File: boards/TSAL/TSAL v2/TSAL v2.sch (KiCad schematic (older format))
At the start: 17 parts, among them Q1 BSS308PE, U1 LR8K4-G, U2 OPA340NA, U3 LTV-356T

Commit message: Changes to TSAL v2
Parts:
- added C1: C_1uF, footprints:C_0805_OEM, symbol C_1uF
- added C2: C_10uF, footprints:C_0805_OEM, symbol C_10uF
- added C?: C_0.1uF, footprints:C_0805_OEM, symbol C_0.1uF
- added C?: C_22uF, footprints:C_1206_OEM, symbol C_22uF
- added C?: C_47uF, footprints:C_0805_OEM, symbol C_47uF
- added D? (x2): LED_0805, footprints:LED_0805_OEM, symbol LED_0805
- added D?: D_Zener_18V, footprints:DO-214AA, symbol D_Zener_18V
- added F?: F_500mA_16V, footprints:Fuse_1210, symbol F_500mA_16V
- added L?: L_4.7uH, footprints:4.7uH_Inductor_OEM, symbol L_4.7uH
- added R11, R12, R?: R_1k, footprints:R_0805_OEM, symbol R_1k
- added R? (x2): R_10k, footprints:R_0805_OEM, symbol R_10k
- added R?: R_55.1k, footprints:R_0805_OEM, symbol R_55.1k
- added R?: R_200, footprints:R_0805_OEM, symbol R_200
- added R?: R_0_Jumper, footprints:R_2512_OEM, symbol R_0_Jumper
- added U?: TPS561201, footprints:SOT-23-6_OEM, symbol TPS561201
- renumbered R11 to R13
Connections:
- net labels added: +12V, 12V_Fused, 5V, VCC
- net labels removed: +5V
- wire segments 58 -> 80
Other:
- note added: "(5V)"
- note added: "12V Indicator"
- note added: "5V Indicator"
- note added: "Add Precision Reference here"
- note added: "BUCK CONVERTER"
- note added: "Use a 100:1 voltage divider here"
- moved on the sheet: D1, R13, R6, U1, U3

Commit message: Final TSAL v2 schematic
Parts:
- removed C?: C_0.1uF, footprints:C_0805_OEM, symbol C_0.1uF
- removed C?: C_22uF, footprints:C_1206_OEM, symbol C_22uF
- removed C?: C_47uF, footprints:C_0805_OEM, symbol C_47uF
- removed D? (x2): LED_0805, footprints:LED_0805_OEM, symbol LED_0805
- removed D?: D_Zener_18V, footprints:DO-214AA, symbol D_Zener_18V
- removed F1: 200mA_Fuse, symbol 200mA_Fuse
- removed F?: F_500mA_16V, footprints:Fuse_1210, symbol F_500mA_16V
- removed L?: L_4.7uH, footprints:4.7uH_Inductor_OEM, symbol L_4.7uH
- removed Q1: BSS308PE, TO_SOT_Packages_SMD:SOT-23, symbol BSS308PE
- removed R1: R_3k_HS, footprints:R_3k_HS_TO247, symbol R_3k_HS
- removed R10: R_2.94M, footprints:R_0805_OEM, symbol R_2.94M
- removed R12, R?: R_1k, footprints:R_0805_OEM, symbol R_1k
- removed R2: R_1k_HS, footprints:R_1k_HS_TO247, symbol R_1k_HS
- removed R3, R4, R5: R_1M, footprints:R_0805_OEM, symbol R_1M
- removed R6, R? (x2): R_10k, footprints:R_0805_OEM, symbol R_10k
- removed R7: R_3.01k, footprints:R_0805_OEM, symbol R_3.01k
- removed R8, R9: R_22M, footprints:R_0805_OEM, symbol R_22M
- removed R?: R_55.1k, footprints:R_0805_OEM, symbol R_55.1k
- removed R?: R_200, footprints:R_0805_OEM, symbol R_200
- removed R?: R_0_Jumper, footprints:R_2512_OEM, symbol R_0_Jumper
- removed U2: OPA340NA, symbol OPA340NA
- removed U?: TPS561201, footprints:SOT-23-6_OEM, symbol TPS561201
- added C2: C_1uF, footprints:C_0805_OEM, symbol C_1uF
- added C3: C_0.1uF, footprints:C_0805_OEM, symbol C_0.1uF
- added F1: F_21mA_420V, footprints:F_21mA_420V, symbol F_21mA_420V
- added J1, J2: Ultrafit_2, footprints:Ultrafit_2, symbol Ultrafit_2
- added J3: micromatch_female_RA_4, footprints:micromatch_female_ra_4, symbol micromatch_female_RA_4
- added Q1: NMOS_GSD_30V, TO_SOT_Packages_SMD:SOT-23, symbol NMOS_GSD_30V
- added R1: R_3k, footprints:R_0805_OEM, symbol R_3k
- added R10: R_499, footprints:R_0805_OEM, symbol R_499
- added R2, R8: R_1k, footprints:R_0805_OEM, symbol R_1k
- added R3, R4, R6: R_270k, footprints:R_0805_OEM, symbol R_270k
- added R5: R_10k, footprints:R_0805_OEM, symbol R_10k
- added R7: R_178k, footprints:R_0805_OEM, symbol R_178k
- added U2: ZXRE160, footprints:ZXRE160, symbol ZXRE160
- added U3: MCP6001RT, footprints:SOT-23-5_OEM, symbol MCP6001RT
- U1: footprint Package_TO_SOT_SMD:TO-252-2 -> TO_SOT_Packages_SMD:TO-252-3_TabPin2; MFN (none) -> Mouser; MPN (none) -> 689-LR8K4-G; Webpage (none) -> https://www.mouser.com/productdetail/?qs=jWmFlM7coATgElKtQd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
- renumbered C2 to C4, R13 to R11, R11 to R9, U3 to U4
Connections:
- net labels removed: +12V, 12V_Fused, 5V
- wire segments 80 -> 77
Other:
- note removed: "(5V)"
- note removed: "12V Indicator"
- note removed: "5V Indicator"
- note removed: "Add Precision Reference here"
- note removed: "BUCK CONVERTER"
- note removed: "Use a 100:1 voltage divider here"
- moved on the sheet: C1, C4, D1, R11, R9, U4

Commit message: Adding TSAL v2 final schematic
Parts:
- J3: symbol micromatch_female_RA_4 -> micromatch_female_RA_4-RESCUE-TSAL_v2
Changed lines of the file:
@@
 $EndComp
 $Comp
-L micromatch_female_RA_4 J3
+L micromatch_female_RA_4-RESCUE-TSAL_v2 J3
 U 1 1 5A73FCF8
 P 10400 2300

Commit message: BOM, Netlist, PCB final
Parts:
- removed J3: micromatch_female_RA_4, footprints:micromatch_female_ra_4, symbol micromatch_female_RA_4-RESCUE-TSAL_v2
- added J3: micromatch_female_TOP_ENTRY_locking_4, footprints:micromatch_female_vert_4, symbol micromatch_female_TOP_ENTRY_locking_4
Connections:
- net VCC is gone; now on net GLV+: U4.4
- net GLV+: now also J3.2, J3.3
- net GND: now also J3.1; no longer C1.2
- net TS-: now also C1.2
- net TSAL-: now also J3.4
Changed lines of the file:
@@
-	1    0    0    -1
-$EndComp
-$Comp
-L GND #PWR03
-U 1 1 5A6AABDC
-P 3850 4900
-F 0 "#PWR03" H 3850 4650 50  0001 C CNN
-F 1 "GND" H 3850 4750 50  0000 C CNN
-F 2 "" H 3850 4900 50  0001 C CNN
-F 3 "" H 3850 4900 50  0001 C CNN
-	1    3850 4900
 	1    0    0    -1
 $EndComp
@@
 5V_TS
 $Comp
-L VCC #PWR04
-U 1 1 5A73F060
-P 12600 3850
-F 0 "#PWR04" H 12600 3700 50  0001 C CNN
-F 1 "VCC" H 12600 4000 50  0000 C CNN
-F 2 "" H 12600 3850 50  0001 C CNN
-F 3 "" H 12600 3850 50  0001 C CNN
-	1    12600 3850
-	1    0    0    -1
-$EndComp
-$Comp
-L micromatch_female_RA_4-RESCUE-TSAL_v2 J3
-U 1 1 5A73FCF8
-P 10400 2300
-F 0 "J3" H 10300 3500 60  0000 C CNN
-F 1 "micromatch_female_RA_4" V 10050 3250 60  0000 C CNN
-F 2 "footprints:micromatch_female_ra_4" H 10200 3400 60  0001 C CNN
-F 3 "" H 10300 3500 60  0001 C CNN
-F 4 "https://www.digikey.com/product-detail/en/te-connectivity-amp-connectors/338070-4/A99482CT-ND/1955784" H 10400 3600 60  0001 C CNN "PurchasingLink"
-F 5 "Digi-Key" H 10500 3700 60  0001 C CNN "MFN"
-F 6 "A99482CT-ND" H 10600 3800 60  0001 C CNN "MPN"
-F 7 "Value" H 10700 3900 60  0001 C CNN "Package"
-	1    10400 2300
-	0    1    1    0
-$EndComp
-$Comp
 L Ultrafit_2 J1
 U 1 1 5A7400DA
@@
 	4100 3800 3950 3800
 Wire Wire Line
-	2200 5700 3000 5700
+	3850 5700 2200 5700
 Wire Wire Line
 	3000 5700 3000 5400
@@
 Connection ~ 3850 4250
 Wire Wire Line
-	3850 4800 3850 4900
+	3850 4800 3850 5700
 Wire Notes Line
 	4800 6650 10100 6650
@@
 	2200 4200 2050 4200
 Wire Wire Line
-	2200 4300 2200 5700
-Wire Wire Line
-	2050 4300 2200 4300
+	2200 5700 2200 4300
+Wire Wire Line
+	2200 4300 2050 4300
 Text GLabel 2200 3050 0    60   Input ~ 0
 TS+
-Text GLabel 10850 2650 0    60   Input ~ 0
+Text GLabel 14150 6700 0    60   Input ~ 0
 TSAL-
 Wire Wire Line
-	10850 2650 11200 2650
-Wire Wire Line
-	11200 2650 11200 2450
-Text GLabel 10850 3000 0    60   Input ~ 0
+	14150 6700 14500 6700
+Wire Wire Line
+	14500 6700 14500 6500
+Text GLabel 14150 7050 0    60   Input ~ 0
 TSAL+
 Wire Wire Line
-	10850 3000 11300 3000
-Wire Wire Line
-	11300 3000 11300 2450
-Text GLabel 11750 3000 2    60   Input ~ 0
+	14150 7050 14600 7050
+Wire Wire Line
+	14600 7050 14600 6500
+Text GLabel 15050 7050 2    60   Input ~ 0
 GLV+
 $Comp
-L GND #PWR05
+L GND #PWR03
 U 1 1 5A741A32
-P 11500 2450
-F 0 "#PWR05" H 11500 2200 50  0001 C CNN
-F 1 "GND" H 11500 2300 50  0000 C CNN
-F 2 "" H 11500 2450 50  0001 C CNN
-F 3 "" H 11500 2450 50  0001 C CNN
-	1    11500 2450
-	1    0    0    -1
-$EndComp
-Wire Wire Line
-	11400 2450 11400 3000
-Wire Wire Line
-	11400 3000 11750 3000
+P 14800 6500
+F 0 "#PWR03" H 14800 6250 50  0001 C CNN
+F 1 "GND" H 14800 6350 50  0000 C CNN
+F 2 "" H 14800 6500 50  0001 C CNN
+F 3 "" H 14800 6500 50  0001 C CNN
+	1    14800 6500
+	1    0    0    -1
+$EndComp
+Wire Wire Line
+	14700 6500 14700 7050
+Wire Wire Line
+	14700 7050 15050 7050
 Wire Notes Line
 	15350 5550 15350 2800
@@
 Connection ~ 10950 4400
 $Comp
-L PWR_FLAG #FLG06
-U 1 1 5A76BFCE
-P 13800 1750
-F 0 "#FLG06" H 13800 1825 50  0001 C CNN
-F 1 "PWR_FLAG" H 13800 1900 50  0000 C CNN
-F 2 "" H 13800 1750 50  0001 C CNN
-F 3 "" H 13800 1750 50  0001 C CNN
-	1    13800 1750
-	1    0    0    -1
-$EndComp
-$Comp
-L VCC #PWR07
-U 1 1 5A76C05D
-P 13800 1750
-F 0 "#PWR07" H 13800 1600 50  0001 C CNN
-F 1 "VCC" H 13800 1900 50  0000 C CNN
-F 2 "" H 13800 1750 50  0001 C CNN
-F 3 "" H 13800 1750 50  0001 C CNN
-	1    13800 1750
-	-1   0    0    1
-$EndComp
-$Comp
-L PWR_FLAG #FLG08
+L PWR_FLAG #FLG04
 U 1 1 5A76C4FF
 P 14200 1750
-F 0 "#FLG08" H 14200 1825 50  0001 C CNN
+F 0 "#FLG04" H 14200 1825 50  0001 C CNN
 F 1 "PWR_FLAG" H 14200 1900 50  0000 C CNN
 F 2 "" H 14200 1750 50  0001 C CNN
@@
 $EndComp
 $Comp
-L PWR_FLAG #FLG09
+L PWR_FLAG #FLG05
 U 1 1 5A76C5DC
 P 14600 1750
-F 0 "#FLG09" H 14600 1825 50  0001 C CNN
+F 0 "#FLG05" H 14600 1825 50  0001 C CNN
 F 1 "PWR_FLAG" H 14600 1900 50  0000 C CNN
 F 2 "" H 14600 1750 50  0001 C CNN
@@
 $EndComp
 $Comp
-L PWR_FLAG #FLG010
+L PWR_FLAG #FLG06
 U 1 1 5A76C632
 P 15000 1750
-F 0 "#FLG010" H 15000 1825 50  0001 C CNN
+F 0 "#FLG06" H 15000 1825 50  0001 C CNN
 F 1 "PWR_FLAG" H 15000 1900 50  0000 C CNN
 F 2 "" H 15000 1750 50  0001 C CNN
@@
 TS+
 $Comp
-L GND #PWR011
+L GND #PWR07
 U 1 1 5A76CA1A
 P 15000 1750
-F 0 "#PWR011" H 15000 1500 50  0001 C CNN
+F 0 "#PWR07" H 15000 1500 50  0001 C CNN
 F 1 "GND" H 15000 1600 50  0000 C CNN
 F 2 "" H 15000 1750 50  0001 C CNN
@@
 	1    0    0    -1
 $EndComp
+$Comp
+L micromatch_female_TOP_ENTRY_locking_4 J3
+U 1 1 5A78D935
+P 14600 6250
+F 0 "J3" H 14600 6650 60  0000 C CNN
+F 1 "micromatch_female_TOP_ENTRY_locking_4" V 14350 6250 60  0000 C CNN
+F 2 "footprints:micromatch_female_vert_4" H 14400 7350 60  0001 C CNN
+F 3 "http://www.te.com/commerce/DocumentDelivery/DDEController?Action=srchrtrv&DocNm=338068&DocType=Customer+Drawing&DocLang=English" H 14500 7450 60  0001 C CNN
+F 4 "https://www.digikey.com/product-detail/en/te-connectivity-amp-connectors/338068-4/A99438CT-ND/1955740" H 14600 7550 60  0001 C CNN "PurchasingLink"
+F 5 "Digi-Key" H 14700 7650 60  0001 C CNN "MFN"
+F 6 "338068-4" H 14800 7750 60  0001 C CNN "MPN"
+F 7 "Value" H 14900 7850 60  0001 C CNN "Package"
+	1    14600 6250
+	0    1    1    0
+$EndComp
+Text GLabel 12600 3850 2    60   Input ~ 0
+GLV+
+Connection ~ 3000 5700
 $EndSCHEMATC

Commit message: Final maybe..?
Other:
- note added: "MISC"
- moved on the sheet: J3
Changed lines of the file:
@@
 Text GLabel 2200 3050 0    60   Input ~ 0
 TS+
-Text GLabel 14150 6700 0    60   Input ~ 0
+Text GLabel 7350 8650 0    60   Input ~ 0
 TSAL-
 Wire Wire Line
-	14150 6700 14500 6700
-Wire Wire Line
-	14500 6700 14500 6500
-Text GLabel 14150 7050 0    60   Input ~ 0
+	7350 8650 7700 8650
+Wire Wire Line
+	7700 8650 7700 8450
+Text GLabel 7350 9000 0    60   Input ~ 0
 TSAL+
 Wire Wire Line
-	14150 7050 14600 7050
-Wire Wire Line
-	14600 7050 14600 6500
-Text GLabel 15050 7050 2    60   Input ~ 0
+	7350 9000 7800 9000
+Wire Wire Line
+	7800 9000 7800 8450
+Text GLabel 8250 9000 2    60   Input ~ 0
 GLV+
 $Comp
 L GND #PWR03
 U 1 1 5A741A32
-P 14800 6500
-F 0 "#PWR03" H 14800 6250 50  0001 C CNN
-F 1 "GND" H 14800 6350 50  0000 C CNN
-F 2 "" H 14800 6500 50  0001 C CNN
-F 3 "" H 14800 6500 50  0001 C CNN
-	1    14800 6500
-	1    0    0    -1
-$EndComp
-Wire Wire Line
-	14700 6500 14700 7050
-Wire Wire Line
-	14700 7050 15050 7050
+P 8000 8450
+F 0 "#PWR03" H 8000 8200 50  0001 C CNN
+F 1 "GND" H 8000 8300 50  0000 C CNN
+F 2 "" H 8000 8450 50  0001 C CNN
+F 3 "" H 8000 8450 50  0001 C CNN
+	1    8000 8450
+	1    0    0    -1
+$EndComp
+Wire Wire Line
+	7900 8450 7900 9000
+Wire Wire Line
+	7900 9000 8250 9000
 Wire Notes Line
 	15350 5550 15350 2800
@@
 L PWR_FLAG #FLG04
 U 1 1 5A76C4FF
-P 14200 1750
-F 0 "#FLG04" H 14200 1825 50  0001 C CNN
-F 1 "PWR_FLAG" H 14200 1900 50  0000 C CNN
-F 2 "" H 14200 1750 50  0001 C CNN
-F 3 "" H 14200 1750 50  0001 C CNN
-	1    14200 1750
+P 9300 8400
+F 0 "#FLG04" H 9300 8475 50  0001 C CNN
+F 1 "PWR_FLAG" H 9300 8550 50  0000 C CNN
+F 2 "" H 9300 8400 50  0001 C CNN
+F 3 "" H 9300 8400 50  0001 C CNN
+	1    9300 8400
 	1    0    0    -1
 $EndComp
@@
 L PWR_FLAG #FLG05
 U 1 1 5A76C5DC
-P 14600 1750
-F 0 "#FLG05" H 14600 1825 50  0001 C CNN
-F 1 "PWR_FLAG" H 14600 1900 50  0000 C CNN
-F 2 "" H 14600 1750 50  0001 C CNN
-F 3 "" H 14600 1750 50  0001 C CNN
-	1    14600 1750
+P 9700 8400
+F 0 "#FLG05" H 9700 8475 50  0001 C CNN
+F 1 "PWR_FLAG" H 9700 8550 50  0000 C CNN
+F 2 "" H 9700 8400 50  0001 C CNN
+F 3 "" H 9700 8400 50  0001 C CNN
+	1    9700 8400
 	1    0    0    -1
 $EndComp
@@
 L PWR_FLAG #FLG06
 U 1 1 5A76C632
-P 15000 1750
-F 0 "#FLG06" H 15000 1825 50  0001 C CNN
-F 1 "PWR_FLAG" H 15000 1900 50  0000 C CNN
-F 2 "" H 15000 1750 50  0001 C CNN
-F 3 "" H 15000 1750 50  0001 C CNN
-	1    15000 1750
-	1    0    0    -1
-$EndComp
-Text GLabel 14600 1750 3    60   Input ~ 0
+P 10100 8400
+F 0 "#FLG06" H 10100 8475 50  0001 C CNN
+F 1 "PWR_FLAG" H 10100 8550 50  0000 C CNN
+F 2 "" H 10100 8400 50  0001 C CNN
+F 3 "" H 10100 8400 50  0001 C CNN
+	1    10100 8400
+	1    0    0    -1
+$EndComp
+Text GLabel 9700 8400 3    60   Input ~ 0
 TS-
-Text GLabel 14200 1750 3    60   Input ~ 0
+Text GLabel 9300 8400 3    60   Input ~ 0
 TS+
 $Comp
 L GND #PWR07
 U 1 1 5A76CA1A
-P 15000 1750
-F 0 "#PWR07" H 15000 1500 50  0001 C CNN
-F 1 "GND" H 15000 1600 50  0000 C CNN
-F 2 "" H 15000 1750 50  0001 C CNN
-F 3 "" H 15000 1750 50  0001 C CNN
-	1    15000 1750
+P 10100 8400
+F 0 "#PWR07" H 10100 8150 50  0001 C CNN
+F 1 "GND" H 10100 8250 50  0000 C CNN
+F 2 "" H 10100 8400 50  0001 C CNN
+F 3 "" H 10100 8400 50  0001 C CNN
+	1    10100 8400
 	1    0    0    -1
 $EndComp
@@
 L micromatch_female_TOP_ENTRY_locking_4 J3
 U 1 1 5A78D935
-P 14600 6250
-F 0 "J3" H 14600 6650 60  0000 C CNN
-F 1 "micromatch_female_TOP_ENTRY_locking_4" V 14350 6250 60  0000 C CNN
-F 2 "footprints:micromatch_female_vert_4" H 14400 7350 60  0001 C CNN
-F 3 "http://www.te.com/commerce/DocumentDelivery/DDEController?Action=srchrtrv&DocNm=338068&DocType=Customer+Drawing&DocLang=English" H 14500 7450 60  0001 C CNN
-F 4 "https://www.digikey.com/product-detail/en/te-connectivity-amp-connectors/338068-4/A99438CT-ND/1955740" H 14600 7550 60  0001 C CNN "PurchasingLink"
-F 5 "Digi-Key" H 14700 7650 60  0001 C CNN "MFN"
-F 6 "338068-4" H 14800 7750 60  0001 C CNN "MPN"
-F 7 "Value" H 14900 7850 60  0001 C CNN "Package"
-	1    14600 6250
+P 7800 8200
+F 0 "J3" H 7800 8600 60  0000 C CNN
+F 1 "micromatch_female_TOP_ENTRY_locking_4" V 7550 8200 60  0000 C CNN
+F 2 "footprints:micromatch_female_vert_4" H 7600 9300 60  0001 C CNN
+F 3 "http://www.te.com/commerce/DocumentDelivery/DDEController?Action=srchrtrv&DocNm=338068&DocType=Customer+Drawing&DocLang=English" H 7700 9400 60  0001 C CNN
+F 4 "https://www.digikey.com/product-detail/en/te-connectivity-amp-connectors/338068-4/A99438CT-ND/1955740" H 7800 9500 60  0001 C CNN "PurchasingLink"
+F 5 "Digi-Key" H 7900 9600 60  0001 C CNN "MFN"
+F 6 "338068-4" H 8000 9700 60  0001 C CNN "MPN"
+F 7 "Value" H 8100 9800 60  0001 C CNN "Package"
+	1    7800 8200
 	0    1    1    0
 $EndComp
@@
 GLV+
 Connection ~ 3000 5700
+Text Notes 8350 7650 0    118  ~ 24
+MISC
+Wire Notes Line
+	6700 7800 10450 7800
+Wire Notes Line
+	10450 7800 10450 9250
+Wire Notes Line
+	10450 9250 6700 9250
+Wire Notes Line
+	6700 9250 6700 7800
 $EndSCHEMATC

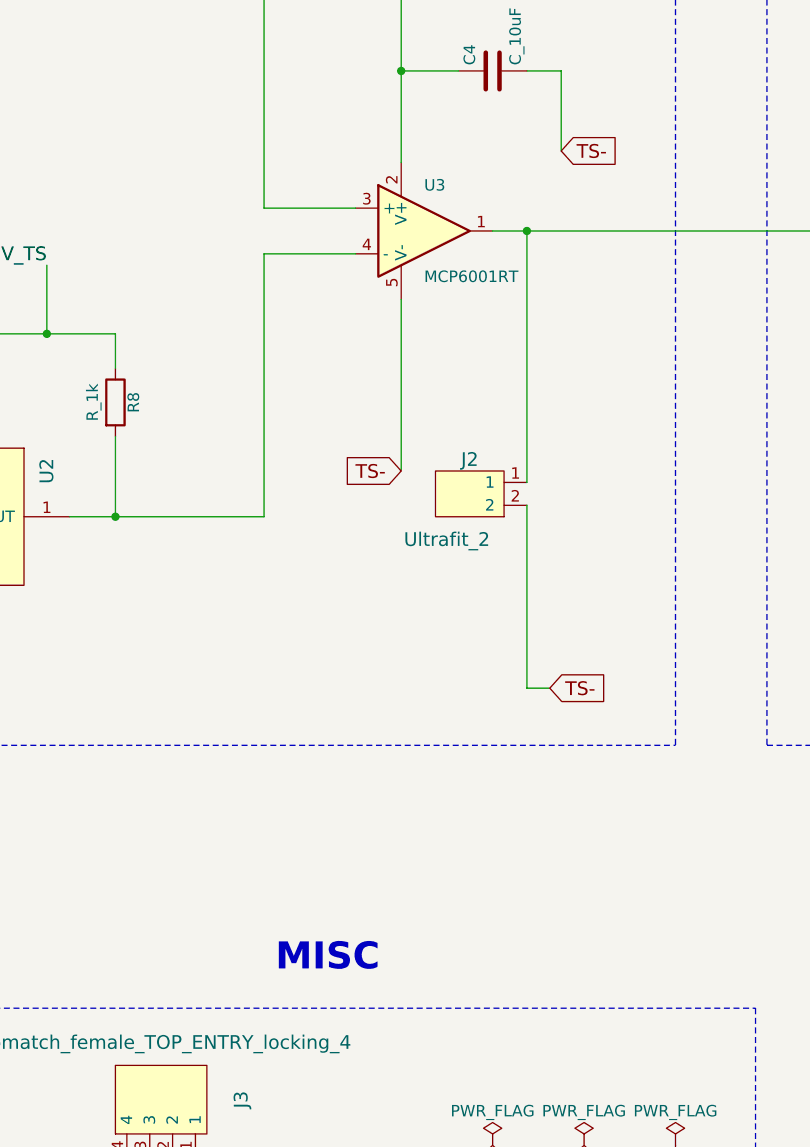
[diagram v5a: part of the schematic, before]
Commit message: Added 1.43k res for AIL
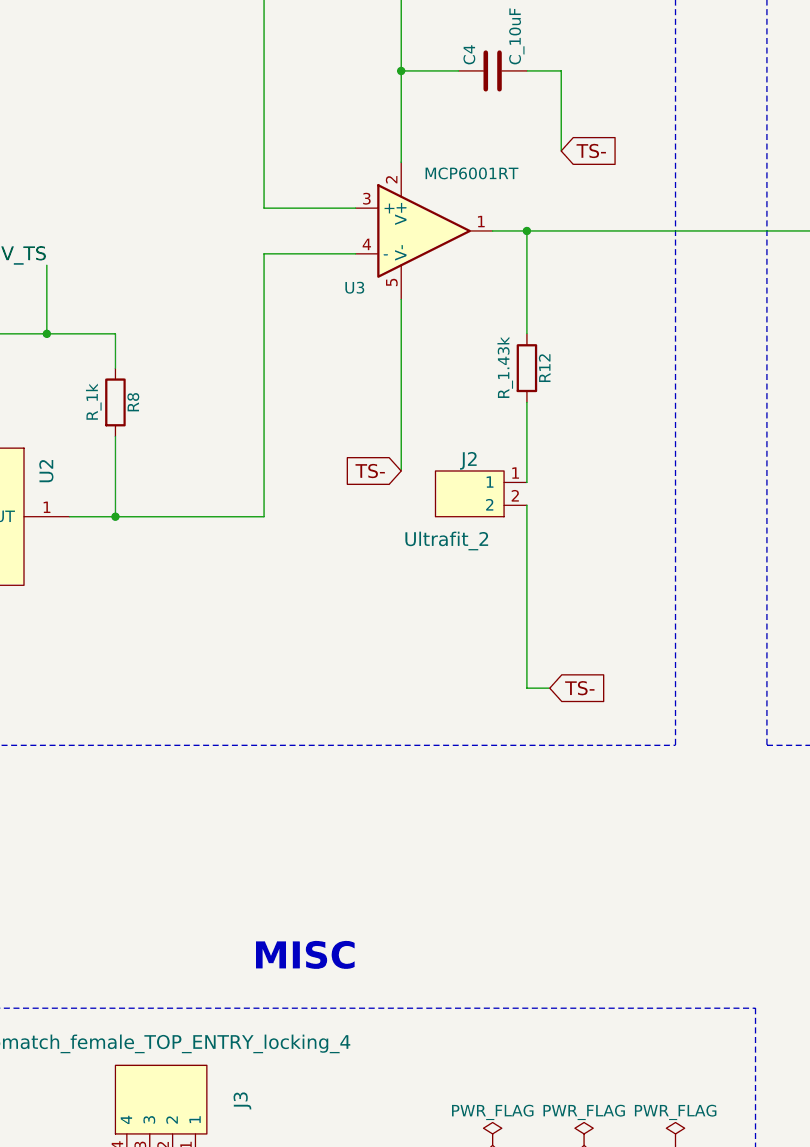
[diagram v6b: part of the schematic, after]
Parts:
- added R12: R_1.43k, footprints:R_0805_OEM, symbol R_1.43k
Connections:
- net at D1.2 (A), R10.2, U3.1: now also R12.1; no longer J2.1
- new net: J2.1, R12.2
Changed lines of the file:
@@
 $EndComp
 $Comp
-L GND #PWR01
+L GND #PWR3
 U 1 1 5A4D7FE1
 P 12600 5250
-F 0 "#PWR01" H 12600 5000 50  0001 C CNN
+F 0 "#PWR3" H 12600 5000 50  0001 C CNN
 F 1 "GND" H 12600 5100 50  0000 C CNN
 F 2 "" H 12600 5250 50  0001 C CNN
@@
 $EndComp
 $Comp
-L GND #PWR02
+L GND #PWR4
 U 1 1 5A4D80CB
 P 14200 4950
-F 0 "#PWR02" H 14200 4700 50  0001 C CNN
+F 0 "#PWR4" H 14200 4700 50  0001 C CNN
 F 1 "GND" H 14200 4800 50  0000 C CNN
 F 2 "" H 14200 4950 50  0001 C CNN
@@
 GLV+
 $Comp
-L GND #PWR03
+L GND #PWR1
 U 1 1 5A741A32
 P 8000 8450
-F 0 "#PWR03" H 8000 8200 50  0001 C CNN
+F 0 "#PWR1" H 8000 8200 50  0001 C CNN
 F 1 "GND" H 8000 8300 50  0000 C CNN
 F 2 "" H 8000 8450 50  0001 C CNN
@@
 Wire Wire Line
 	7000 2550 7150 2550
-Wire Wire Line
-	9450 5500 9450 4400
 Connection ~ 9450 4400
 Wire Wire Line
@@
 Connection ~ 10950 4400
 $Comp
-L PWR_FLAG #FLG04
+L PWR_FLAG #FLG1
 U 1 1 5A76C4FF
 P 9300 8400
-F 0 "#FLG04" H 9300 8475 50  0001 C CNN
+F 0 "#FLG1" H 9300 8475 50  0001 C CNN
 F 1 "PWR_FLAG" H 9300 8550 50  0000 C CNN
 F 2 "" H 9300 8400 50  0001 C CNN
@@
 $EndComp
 $Comp
-L PWR_FLAG #FLG05
+L PWR_FLAG #FLG2
 U 1 1 5A76C5DC
 P 9700 8400
-F 0 "#FLG05" H 9700 8475 50  0001 C CNN
+F 0 "#FLG2" H 9700 8475 50  0001 C CNN
 F 1 "PWR_FLAG" H 9700 8550 50  0000 C CNN
 F 2 "" H 9700 8400 50  0001 C CNN
@@
 $EndComp
 $Comp
-L PWR_FLAG #FLG06
+L PWR_FLAG #FLG3
 U 1 1 5A76C632
 P 10100 8400
-F 0 "#FLG06" H 10100 8475 50  0001 C CNN
+F 0 "#FLG3" H 10100 8475 50  0001 C CNN
 F 1 "PWR_FLAG" H 10100 8550 50  0000 C CNN
 F 2 "" H 10100 8400 50  0001 C CNN
@@
 TS+
 $Comp
-L GND #PWR07
+L GND #PWR2
 U 1 1 5A76CA1A
 P 10100 8400
-F 0 "#PWR07" H 10100 8150 50  0001 C CNN
+F 0 "#PWR2" H 10100 8150 50  0001 C CNN
 F 1 "GND" H 10100 8250 50  0000 C CNN
 F 2 "" H 10100 8400 50  0001 C CNN
@@
 U 1 1 5A775866
 P 9000 4400
-F 0 "U3" H 9000 4600 50  0000 L CNN
-F 1 "MCP6001RT" H 9000 4200 50  0000 L CNN
+F 0 "U3" H 8650 4150 50  0000 L CNN
+F 1 "MCP6001RT" H 9000 4650 50  0000 L CNN
 F 2 "footprints:SOT-23-5_OEM" H 8900 4500 50  0001 C CNN
 F 3 "http://ww1.microchip.com/downloads/en/DeviceDoc/21733j.pdf" H 9000 4600 50  0001 C CNN
@@
 GLV+
 Connection ~ 3000 5700
-Text Notes 8350 7650 0    118  ~ 24
+Text Notes 8250 7650 0    118  ~ 24
 MISC
 Wire Notes Line
@@
 Wire Notes Line
 	6700 9250 6700 7800
+$Comp
+L R_1.43k R12
+U 1 1 5A7BCAC8
+P 9450 5000
+F 0 "R12" V 9530 5000 50  0000 C CNN
+F 1 "R_1.43k" V 9350 5000 50  0000 C CNN
+F 2 "footprints:R_0805_OEM" H 9250 5300 50  0001 C CNN
+F 3 "https://media.digikey.com/pdf/Data%20Sheets/Tyco%20Electonics%20AMP%20PDFs/RN73_Series_2011.pdf" H 9500 4700 50  0001 C CNN
+F 4 "Digi-Key" H 9450 4500 60  0001 C CNN "MFN"
+F 5 "A103351CT-ND" H 9450 4600 60  0001 C CNN "MPN"
+F 6 "https://www.digikey.com/product-detail/en/te-connectivity-passive-product/RN73C2A1K43BTDF/A103351CT-ND/2730566" H 9930 5400 60  0001 C CNN "PurchasingLink"
+	1    9450 5000
+	1    0    0    -1
+$EndComp
+Wire Wire Line
+	9450 5150 9450 5500
+Wire Wire Line
+	9450 4850 9450 4400
 $EndSCHEMATC
